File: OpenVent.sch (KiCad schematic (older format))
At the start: 0 parts

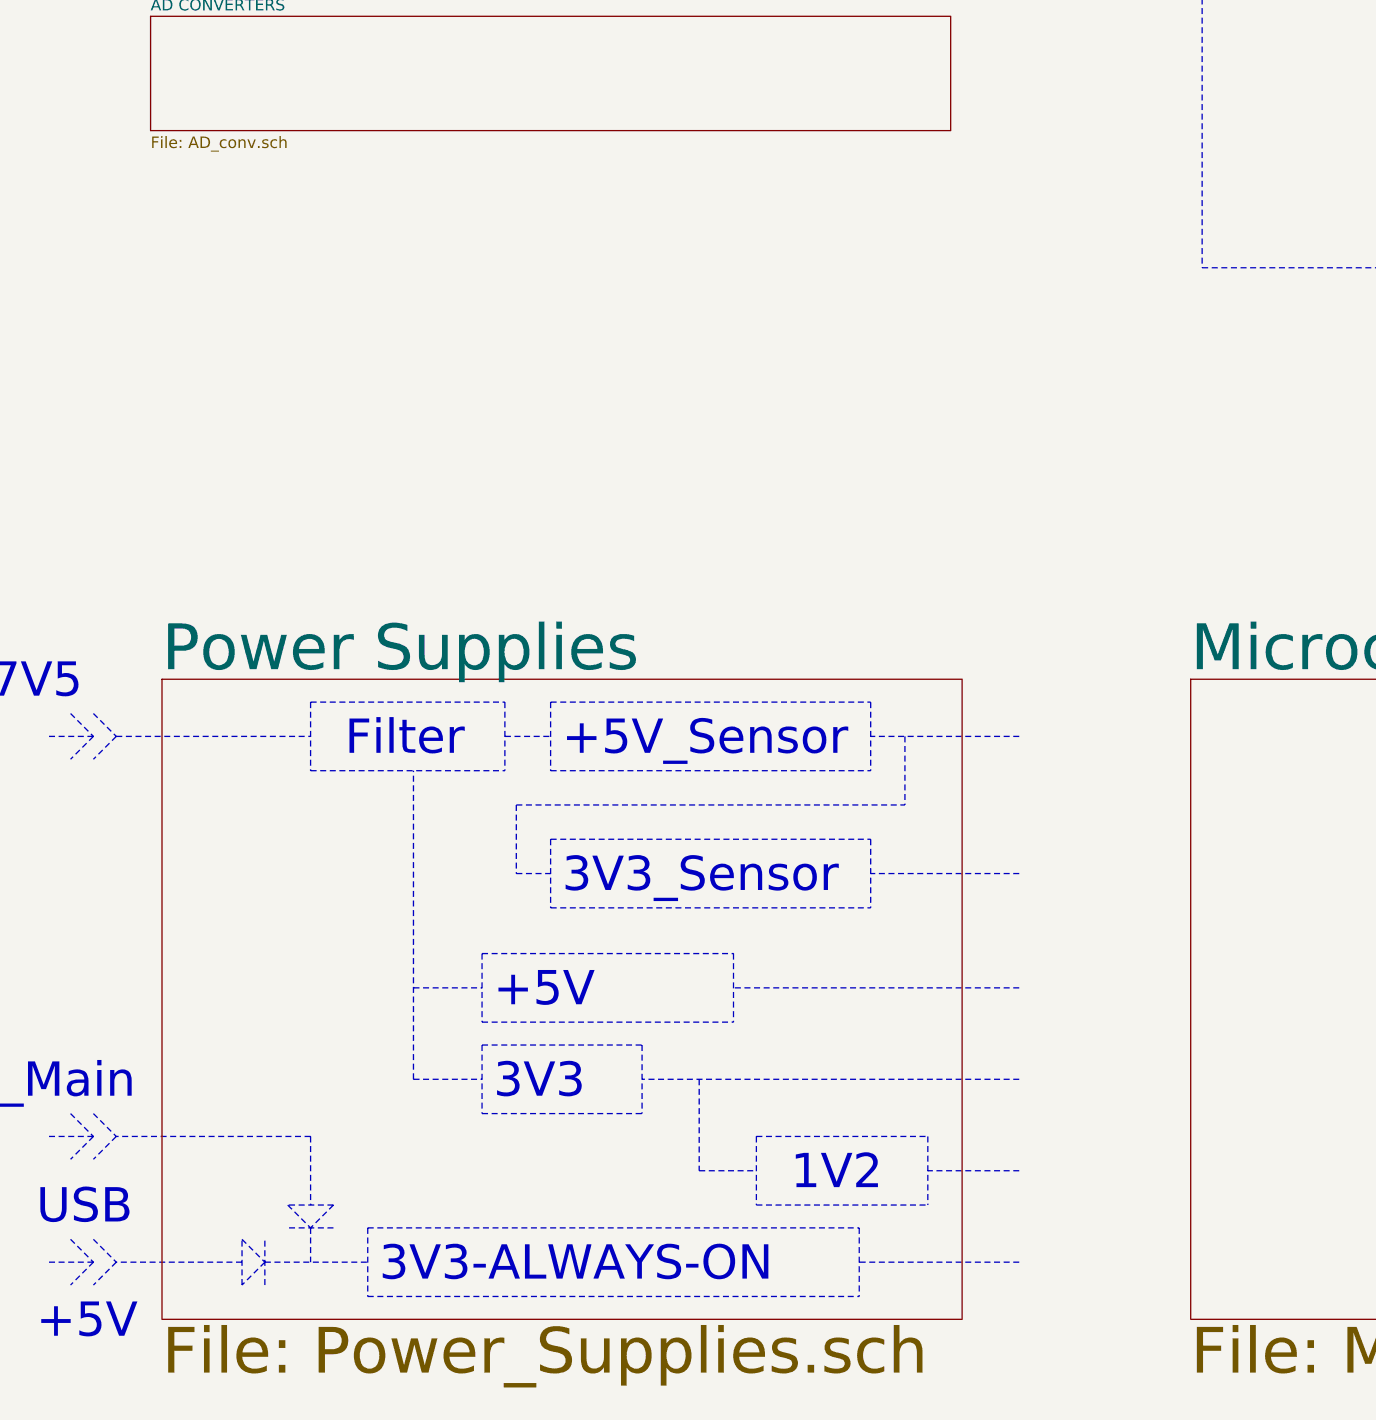
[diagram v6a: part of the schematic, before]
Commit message: Replaced front sheet, added Speaker_Driver sheet
New front sheet provided by Rick on 02/04/2021 with re-ordered pages and addition of Speaker_Driver
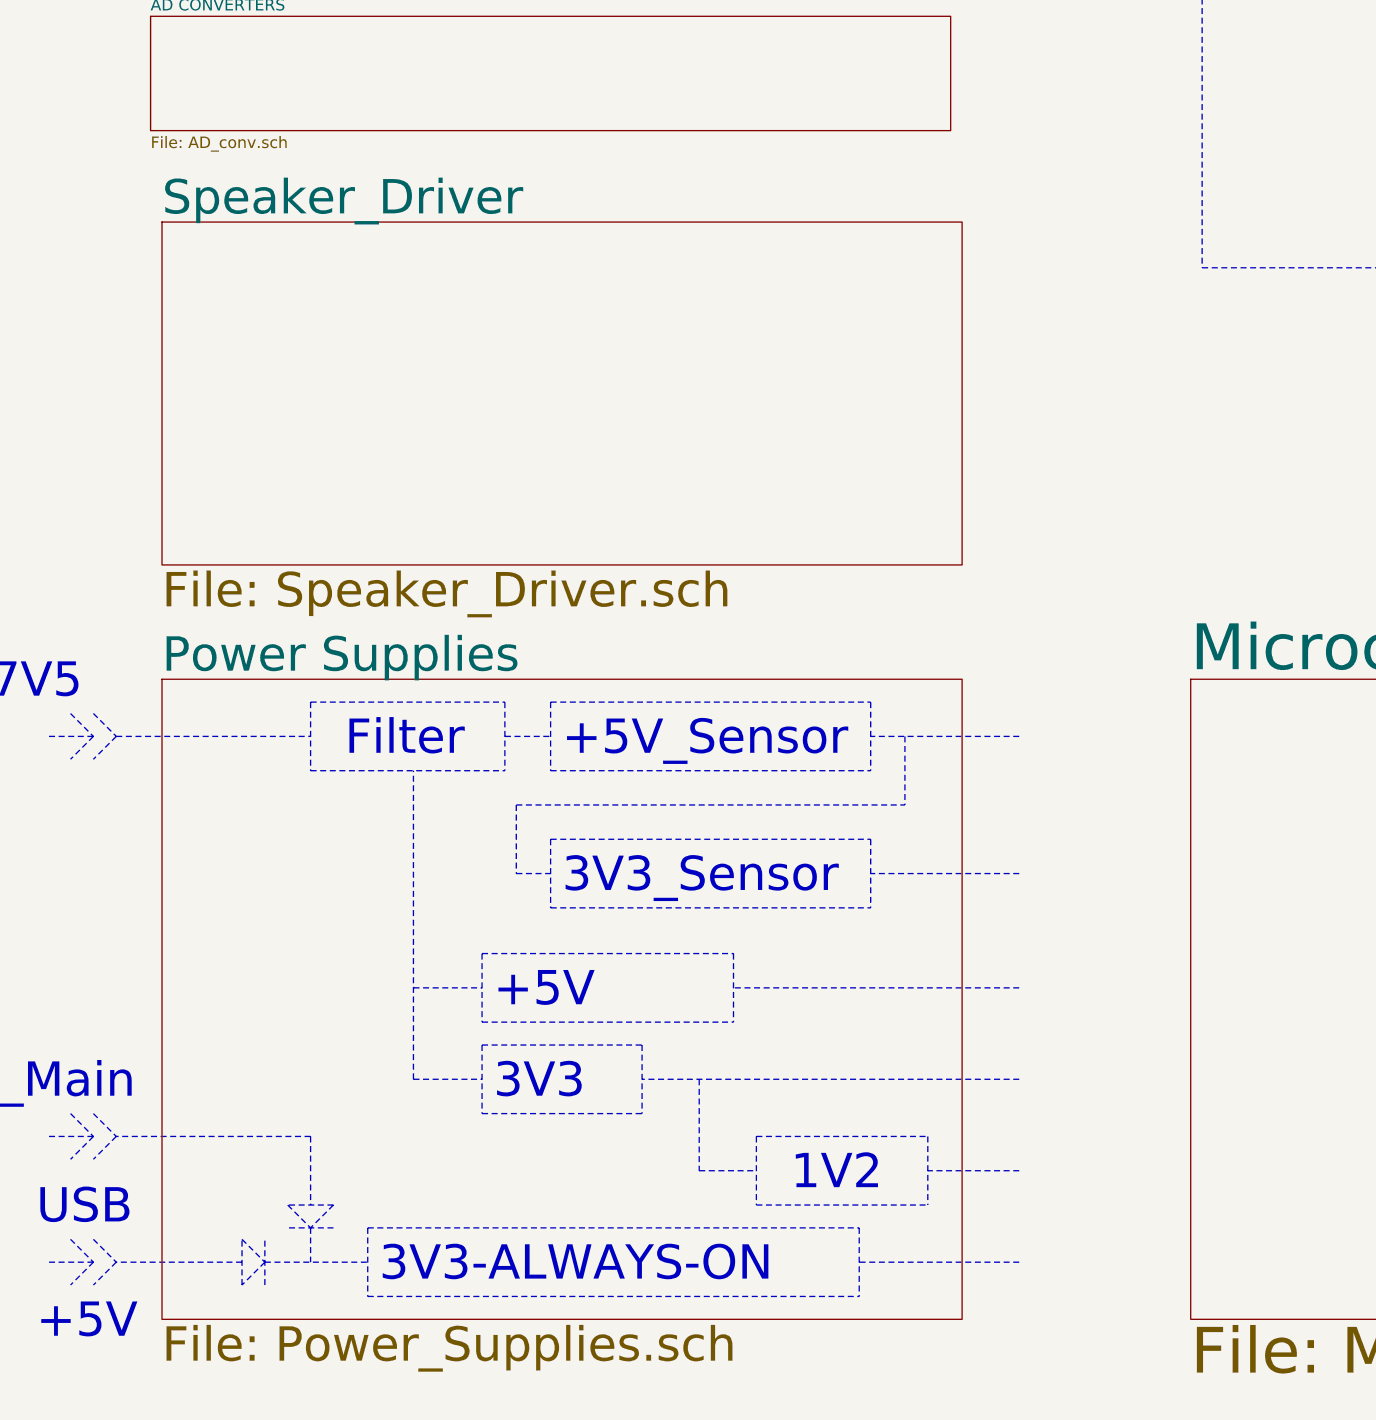
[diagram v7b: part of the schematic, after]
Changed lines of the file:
@@
 $Descr A3 16535 11693
 encoding utf-8
-Sheet 1 8
+Sheet 1 9
 Title "OpenVent Control Board"
 Date "2020-10-20"
@@
 Text Notes 12650 2200 0    100  ~ 0
 4.65x
+Wire Notes Line style solid
+	12000 9000 9000 9000
+Text Notes 10150 8950 0    150  ~ 0
+JTAG
+Wire Notes Line style solid
+	12800 7250 12800 8250
+Wire Notes Line style solid
+	14000 7250 14000 8250
+Wire Notes Line style solid
+	12800 7250 14000 7250
+Text Notes 13150 7950 0    150  ~ 0
+FTDI\nJTAG
+Wire Notes Line style solid
+	12800 8250 14000 8250
+Wire Notes Line style solid
+	15600 7650 15500 7750
+Wire Notes Line style solid
+	15500 7750 15600 7850
+Wire Notes Line style solid
+	15500 7650 15400 7750
+Wire Notes Line style solid
+	15400 7750 15500 7850
+Text Notes 14800 7650 0    150  ~ 0
+USB-JTAG
+Wire Notes Line style solid
+	15700 7750 15500 7750
+Wire Notes Line style solid
+	14000 7750 15400 7750
+Wire Notes Line style solid
+	12400 8000 12400 8600
+Wire Notes Line style solid
+	11600 8000 12400 8000
+Wire Notes Line style solid
+	11600 8000 11600 8600
+Wire Notes Line style solid
+	11600 8600 12400 8600
+Text Notes 11750 8400 0    150  ~ 0
+BUF
+Wire Notes Line style solid
+	12400 6900 12400 7500
+Wire Notes Line style solid
+	11600 6900 12400 6900
+Wire Notes Line style solid
+	11600 6900 11600 7500
+Wire Notes Line style solid
+	11600 7500 12400 7500
+Text Notes 11750 7300 0    150  ~ 0
+BUF
+Wire Notes Line style solid
+	12000 7750 12800 7750
+Wire Notes Line style solid
+	12000 7500 12000 8000
+Wire Notes Line style solid
+	12000 8600 12000 9000
+Wire Notes Line style solid
+	12000 5750 12000 6900
+Wire Notes Line style solid
+	12000 5750 7750 5750
+Wire Notes Line style solid
+	7000 1250 7000 3700
+Wire Notes Line style solid
+	9000 1250 9000 3700
+Wire Notes Line style solid
+	7000 1250 9000 1250
+Wire Notes Line style solid
+	8250 850  8250 1250
+Text Notes 7750 2300 0    150  ~ 0
+FPGA
+Wire Notes Line style solid
+	7750 3700 7750 5750
+Wire Notes Line style solid
+	7000 8100 7000 10500
+$Sheet
+S 1500 1000 3500 2800
+U 5FCA4074
+F0 "UI" 200
+F1 "UI.sch" 200
+$EndSheet
+$Sheet
+S 6400 1000 3500 2800
+U 5F8F894A
+F0 "FPGA" 200
+F1 "FPGA.sch" 200
+$EndSheet
+Wire Notes Line style solid
+	7250 3700 7250 8100
+Wire Notes Line style solid
+	10000 10250 9000 10250
+Wire Notes Line style solid
+	7000 8100 9000 8100
+Wire Notes Line style solid
+	7000 10500 9000 10500
+Wire Notes Line style solid
+	9000 8100 9000 10500
+Wire Notes Line style solid
+	9000 3000 15400 3000
+Wire Notes Line style solid
+	7000 3700 9000 3700
+Wire Notes Line style solid
+	9100 6750 9100 7350
+Wire Notes Line style solid
+	8300 6750 9100 6750
+Wire Notes Line style solid
+	8300 6750 8300 7350
+Wire Notes Line style solid
+	8300 7350 9100 7350
+Text Notes 8450 7150 0    150  ~ 0
+BUF
+Wire Notes Line style solid
+	8700 7350 8700 8100
+Wire Notes Line style solid
+	8700 3700 8700 4450
+Wire Notes Line style solid
+	11150 7600 11350 7600
+Wire Notes Line style solid
+	11150 7600 11150 7900
+Wire Notes Line style solid
+	11350 7600 11350 7900
+Wire Notes Line style solid
+	11150 7900 11350 7900
+Wire Notes Line style solid
+	11250 7200 11250 7600
+Wire Notes Line style solid
+	11600 7200 11250 7200
+Wire Notes Line style solid
+	11250 7900 11250 8300
+Wire Notes Line style solid
+	11600 8300 11250 8300
+Text Notes 11350 7850 0    150  ~ 0
+JMPR
+$Sheet
+S 1450 5100 3500 500
+U 601B7AF8
+F0 "AD CONVERTERS" 50
+F1 "AD_conv.sch" 50
+$EndSheet
 $Sheet
 S 11000 1000 3500 2800
@@
 $EndSheet
 Wire Notes Line style solid
-	12000 9000 9000 9000
-Text Notes 10150 8950 0    150  ~ 0
-JTAG
-Wire Notes Line style solid
-	12800 7250 12800 8250
-Wire Notes Line style solid
-	14000 7250 14000 8250
-Wire Notes Line style solid
-	12800 7250 14000 7250
-Text Notes 13150 7950 0    150  ~ 0
-FTDI\nJTAG
-Wire Notes Line style solid
-	12800 8250 14000 8250
-Wire Notes Line style solid
-	15600 7650 15500 7750
-Wire Notes Line style solid
-	15500 7750 15600 7850
-Wire Notes Line style solid
-	15500 7650 15400 7750
-Wire Notes Line style solid
-	15400 7750 15500 7850
-Text Notes 14800 7650 0    150  ~ 0
-USB-JTAG
-Wire Notes Line style solid
-	15700 7750 15500 7750
-Wire Notes Line style solid
-	14000 7750 15400 7750
-Wire Notes Line style solid
-	12400 8000 12400 8600
-Wire Notes Line style solid
-	11600 8000 12400 8000
-Wire Notes Line style solid
-	11600 8000 11600 8600
-Wire Notes Line style solid
-	11600 8600 12400 8600
-Text Notes 11750 8400 0    150  ~ 0
-BUF
-Wire Notes Line style solid
-	12400 6900 12400 7500
-Wire Notes Line style solid
-	11600 6900 12400 6900
-Wire Notes Line style solid
-	11600 6900 11600 7500
-Wire Notes Line style solid
-	11600 7500 12400 7500
-Text Notes 11750 7300 0    150  ~ 0
-BUF
-Wire Notes Line style solid
-	12000 7750 12800 7750
-Wire Notes Line style solid
-	12000 7500 12000 8000
-Wire Notes Line style solid
-	12000 8600 12000 9000
-Wire Notes Line style solid
-	12000 5750 12000 6900
-Wire Notes Line style solid
-	12000 5750 7750 5750
-Wire Notes Line style solid
-	7000 1250 7000 3700
-Wire Notes Line style solid
-	9000 1250 9000 3700
-Wire Notes Line style solid
-	7000 1250 9000 1250
-Wire Notes Line style solid
-	8250 850  8250 1250
-Text Notes 7750 2300 0    150  ~ 0
-FPGA
-Wire Notes Line style solid
-	7750 3700 7750 5750
-Wire Notes Line style solid
-	7000 8100 7000 10500
-$Sheet
-S 6400 1000 3500 2800
-U 5F8F894A
-F0 "FPGA" 200
-F1 "FPGA.sch" 200
-$EndSheet
-Wire Notes Line style solid
-	7250 3700 7250 8100
-Wire Notes Line style solid
-	10000 10250 9000 10250
-Wire Notes Line style solid
-	7000 8100 9000 8100
-Wire Notes Line style solid
-	7000 10500 9000 10500
-Wire Notes Line style solid
-	9000 8100 9000 10500
-Wire Notes Line style solid
-	9000 3000 15400 3000
-Wire Notes Line style solid
-	7000 3700 9000 3700
-Wire Notes Line style solid
-	9100 6750 9100 7350
-Wire Notes Line style solid
-	8300 6750 9100 6750
-Wire Notes Line style solid
-	8300 6750 8300 7350
-Wire Notes Line style solid
-	8300 7350 9100 7350
-Text Notes 8450 7150 0    150  ~ 0
-BUF
-Wire Notes Line style solid
-	8700 7350 8700 8100
-Wire Notes Line style solid
-	8700 3700 8700 4450
-Wire Notes Line style solid
-	11150 7600 11350 7600
-Wire Notes Line style solid
-	11150 7600 11150 7900
-Wire Notes Line style solid
-	11350 7600 11350 7900
-Wire Notes Line style solid
-	11150 7900 11350 7900
-Wire Notes Line style solid
-	11250 7200 11250 7600
-Wire Notes Line style solid
-	11600 7200 11250 7200
-Wire Notes Line style solid
-	11250 7900 11250 8300
-Wire Notes Line style solid
-	11600 8300 11250 8300
-Text Notes 11350 7850 0    150  ~ 0
-JMPR
-$Sheet
-S 1450 5100 3500 500
-U 601B7AF8
-F0 "AD CONVERTERS" 50
-F1 "AD_conv.sch" 50
-$EndSheet
-Wire Notes Line style solid
 	2600 9350 2900 9350
 Wire Notes Line style solid
@@
 Wire Notes Line style solid
 	1200 8250 1000 8250
-$Sheet
-S 1500 1000 3500 2800
-U 5FCA4074
-F0 "UI" 200
-F1 "UI.sch" 200
-$EndSheet
-$Sheet
-S 1500 8000 3500 2800
-U 5F99D63D
-F0 "Power Supplies" 200
-F1 "Power_Supplies.sch" 200
-$EndSheet
 Wire Notes Line style solid
 	2900 1500 2900 2100
@@
 Text Notes 3350 4300 0    150  ~ 0
 PB_Select
+$Sheet
+S 1500 6000 3500 1500
+U 606B52C8
+F0 "Speaker_Driver" 150
+F1 "Speaker_Driver.sch" 150
+$EndSheet
+$Sheet
+S 1500 8000 3500 2800
+U 6070CFE3
+F0 "Power Supplies" 150
+F1 "Power_Supplies.sch" 150
+$EndSheet
 $EndSCHEMATC

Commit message: Updated front sheet with schematic provided by Rick 07-04-21 21:08 BST
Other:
- note added: "Analog\n to\nDigital"
- note added: "DRIVER"
- note added: "Sel\nJMPR"
- note added: "UI"
- note removed: "JMPR"
- note removed: "Vbatt"
